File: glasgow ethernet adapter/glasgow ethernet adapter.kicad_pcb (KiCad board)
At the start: 4 copper layers, 61.7 x 49 mm, 59 parts, among them J1 Glasgow Port, J2 RJ45_Amphenol_RJMG201K21120FR, U1 MxL86110, Y1 25 MHz

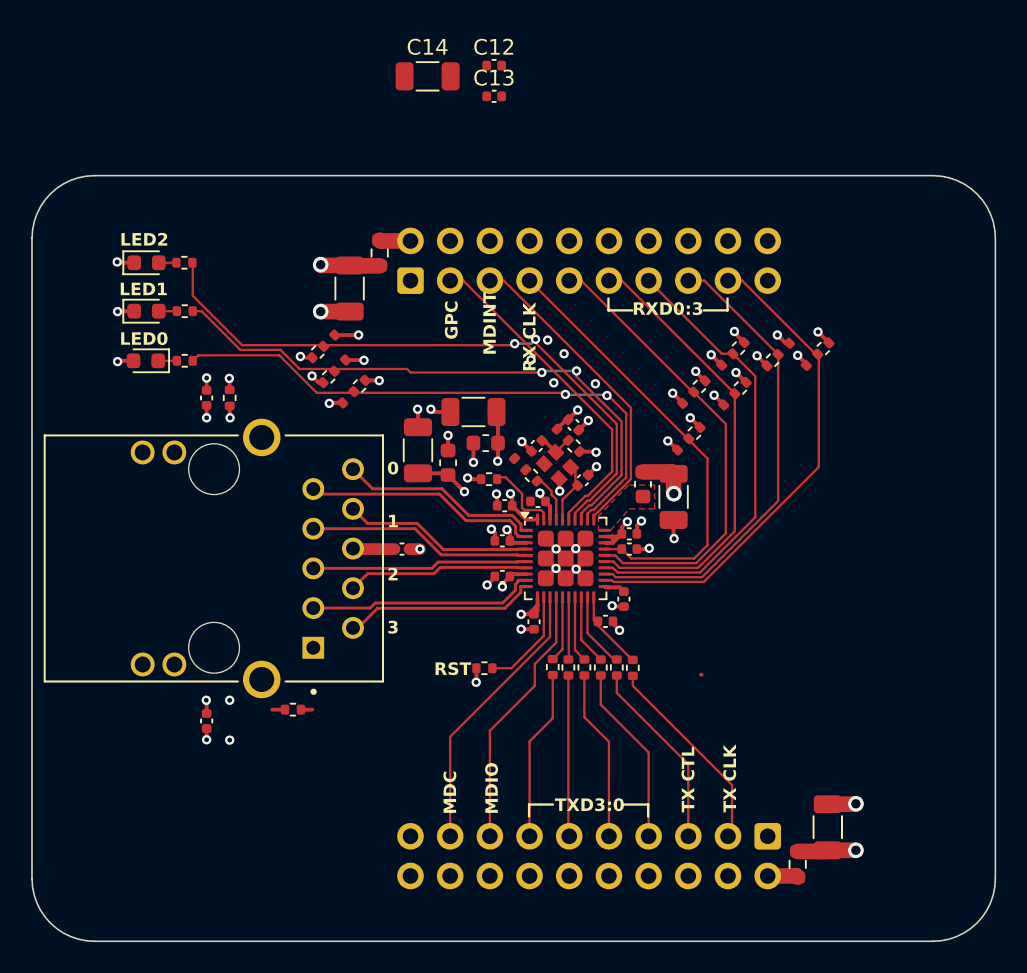
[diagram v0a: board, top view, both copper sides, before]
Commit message: remove configurable pulls on LEDs
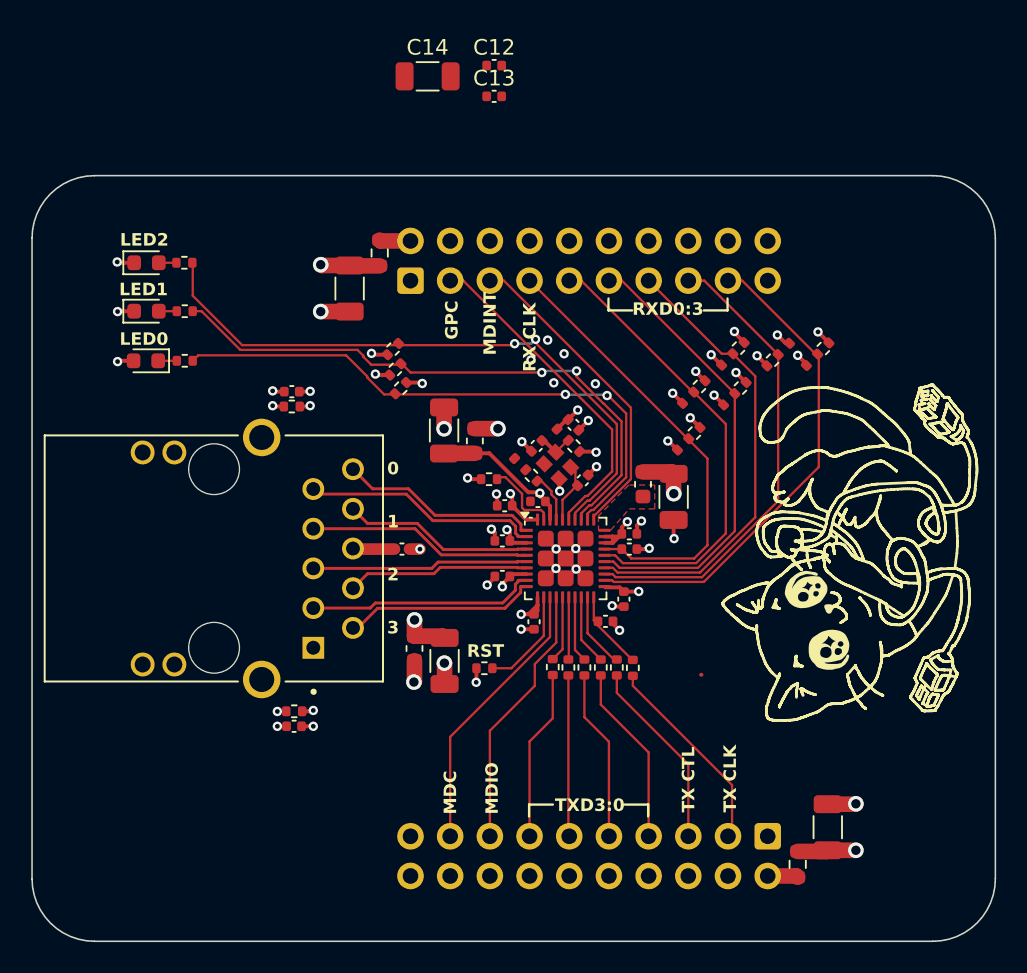
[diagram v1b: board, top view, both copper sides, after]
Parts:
- added REF**: cat, glasgow:cat, F.Cu at (181.5, 100.0)
- R3, R6, R9: footprint glasgow:R-3-Way_0402_1005Metric -> Resistor_SMD:R_0402_1005Metric
- moved C15 13.6 mm to (154.8, 106.6), turned to -90 degrees
- moved L2 12.1 mm to (152.8, 105.8), turned to 90 degrees
- moved C22 5.61 mm to (145.1, 110.7), turned to 0 degrees
- moved C27 5.46 mm to (145.0, 89.3), turned to 0 degrees
- moved R6 4.81 mm to (151.4, 86.6), turned to -135 degrees
- moved R3 4.29 mm to (151.6, 87.9), turned to -135 degrees
- moved R24 4.01 mm to (145.0, 90.3), turned to 0 degrees
- moved R9 2.65 mm to (151.9, 89.1), turned to 45 degrees
- moved C11 2.22 mm to (154.7, 91.8), turned to 90 degrees
- moved L3 0.71 mm to (156.7, 92.5), turned to -90 degrees
- moved R10 0.13 mm to (145.1, 109.8)
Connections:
- R3 pad 1: GND -> /CFG_LDO0
- R3 pad 2: /CFG_LDO0 -> GND
- R6 pad 1: GND -> /CFG_LDO1
- R6 pad 2: /CFG_LDO1 -> GND
- R9 pad 1: +3V3 -> /CFG_EXT
- R9 pad 2: /CFG_EXT -> +3V3
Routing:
- net +1V1: track 5.95 -> 27.1 mm, vias 2 -> 3
- net +3V3: track 25.5 -> 23.3 mm, vias 16 -> 14
- net C_GND: track 3.38 -> 2.59 mm
- net /AVDDL: track 19.5 -> 20.0 mm, vias 4 -> 3
- net GND: track 45.1 -> 44.9 mm, vias 44 -> 43
- removed copper zone on In2.Cu, net +1V1

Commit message: move things around
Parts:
- moved C13 53.2 mm to (178.6, 119.5), turned to -90 degrees
- moved C14 33.2 mm to (170.7, 97.7)
- moved C12 15.9 mm to (149.4, 81.9), turned to -90 degrees
- moved R11 5.74 mm to (153.6, 111.4)
- moved R9 5.05 mm to (147.9, 86.1), turned to 135 degrees
- moved C11 2.94 mm to (154.8, 94.8), turned to -90 degrees
- moved R6 2.88 mm to (150.1, 84.1), turned to 45 degrees
- moved R3 2.77 mm to (150.2, 85.5)
- moved C20 2.30 mm to (146.5, 81.9), turned to 180 degrees
- moved C10 1.41 mm to (170.6, 95.3), turned to 0 degrees
- moved C17 0.98 mm to (180.2, 117.2)
- moved L1 0.05 mm to (167.5, 95.2)
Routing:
- net +3V3: track 23.3 -> 36.0 mm, vias 14 -> 15
- net Net-(U1-RSTN): track 6.61 -> 12.2 mm
- net /PHYAD1: track 28.9 -> 33.7 mm
- net GND: track 44.9 -> 48.5 mm, vias 43 -> 47
- net +1V1: track 27.1 -> 30.4 mm
- net /RXD0: track 29.4 -> 32.6 mm
- net /RXD1: track 29.6 -> 32.8 mm
- net /PHYAD2: track 29.6 -> 32.4 mm
- net /PLLOFF: track 30.3 -> 32.9 mm
- net /AVDDL: track 20.0 -> 17.9 mm
- net /PHYAD0: track 31.7 -> 32.9 mm
- net Net-(R26-Pad2): track 0.15 -> 1.36 mm

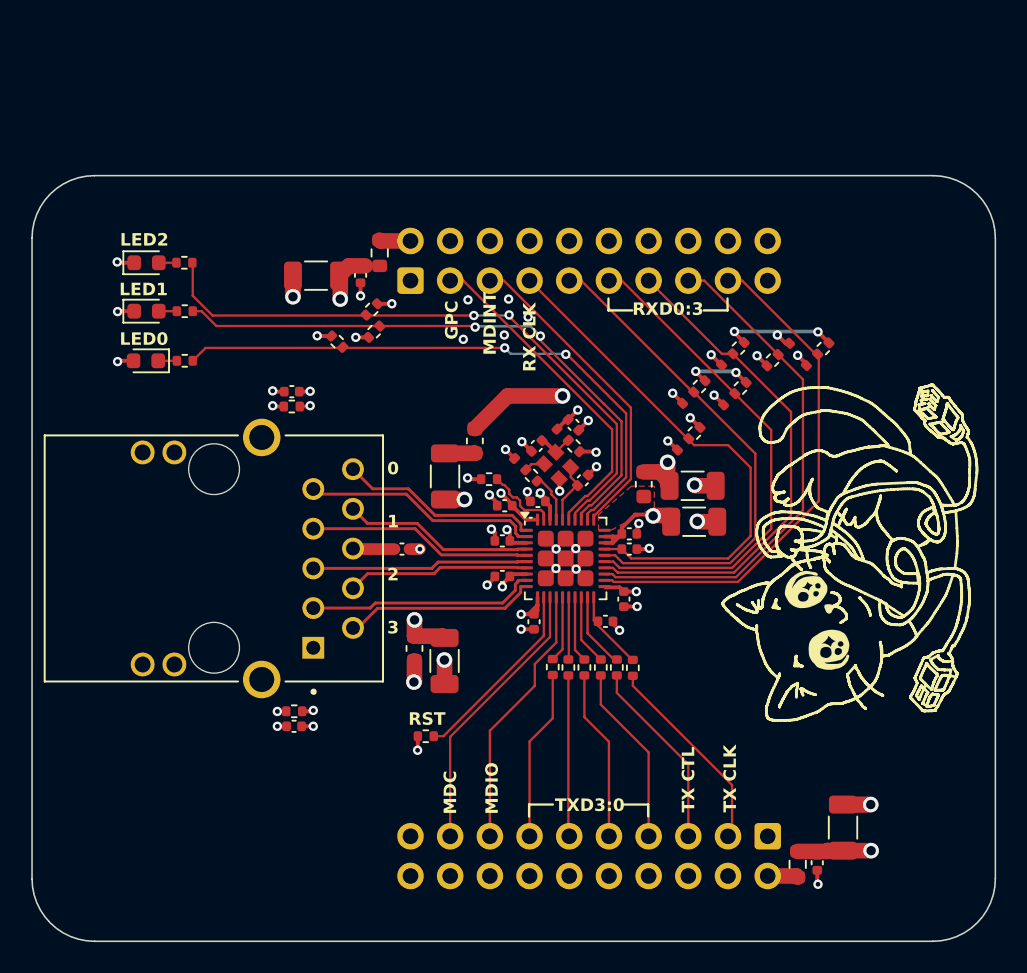
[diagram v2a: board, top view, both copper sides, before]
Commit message: increase fab tolerances, DRC fixes
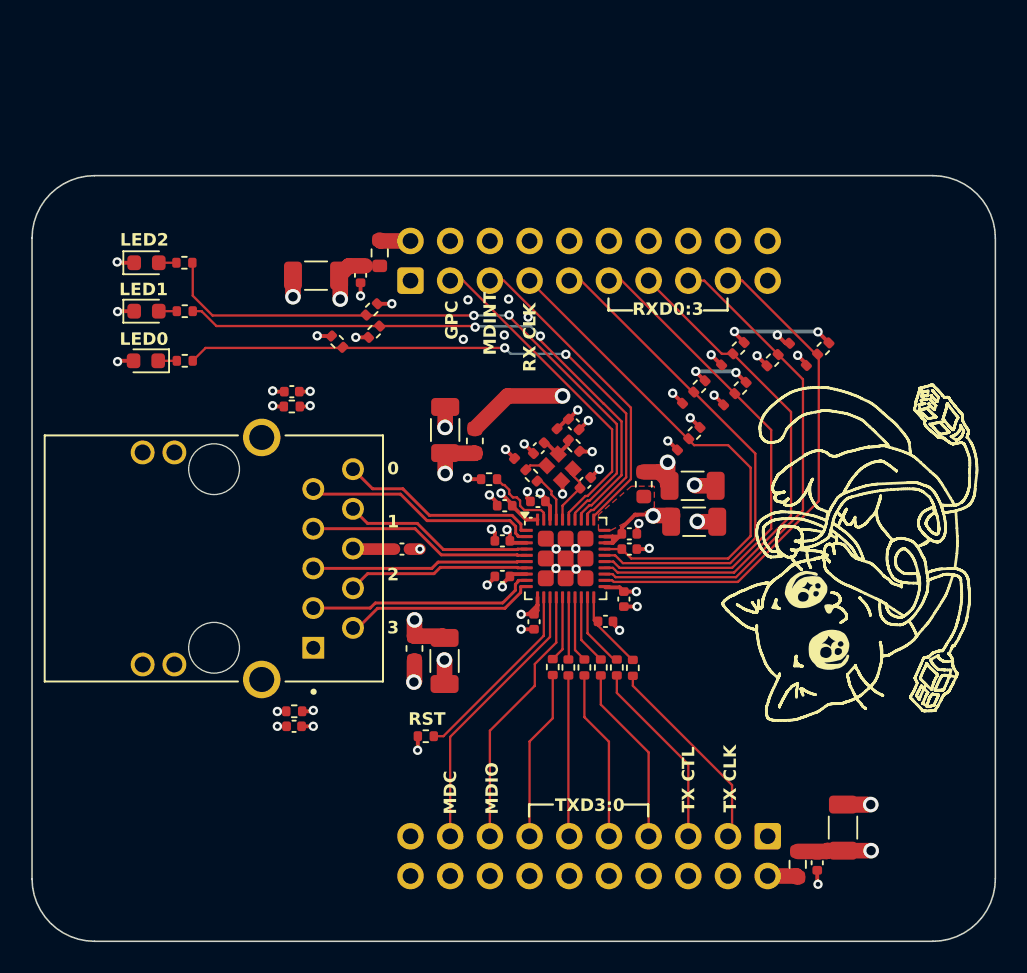
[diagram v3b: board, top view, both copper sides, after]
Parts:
- moved C11 2.97 mm to (154.8, 91.8), turned to 90 degrees
- moved C25 0.23 mm to (163.8, 95.2)
- moved Y1 0.20 mm to (162.1, 94.2)
- moved C26 0.19 mm to (160.8, 92.9)
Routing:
- net /AVDDL: track 17.9 -> 26.7 mm, vias 3 -> 4
- net C_GND: track 2.59 -> 3.16 mm

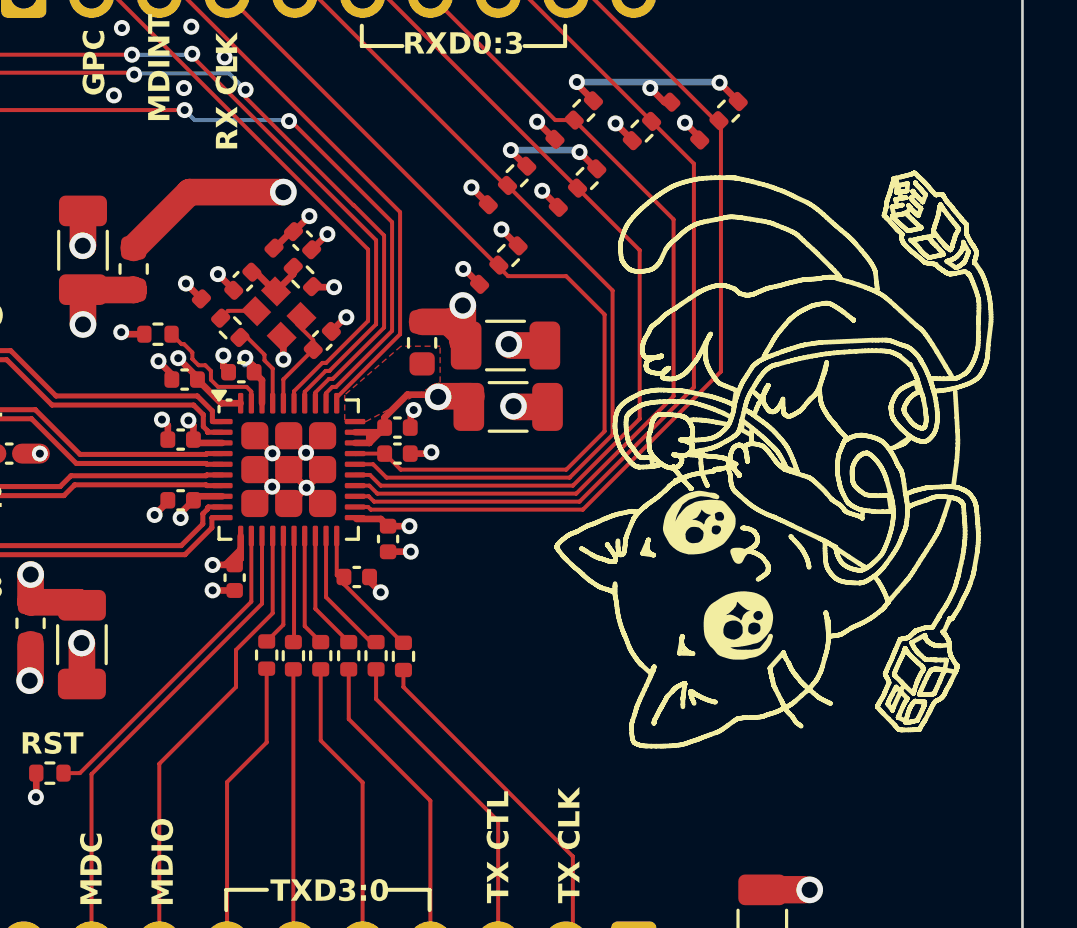
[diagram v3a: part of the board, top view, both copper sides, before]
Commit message: export fab outputs, add note on parts sourcing
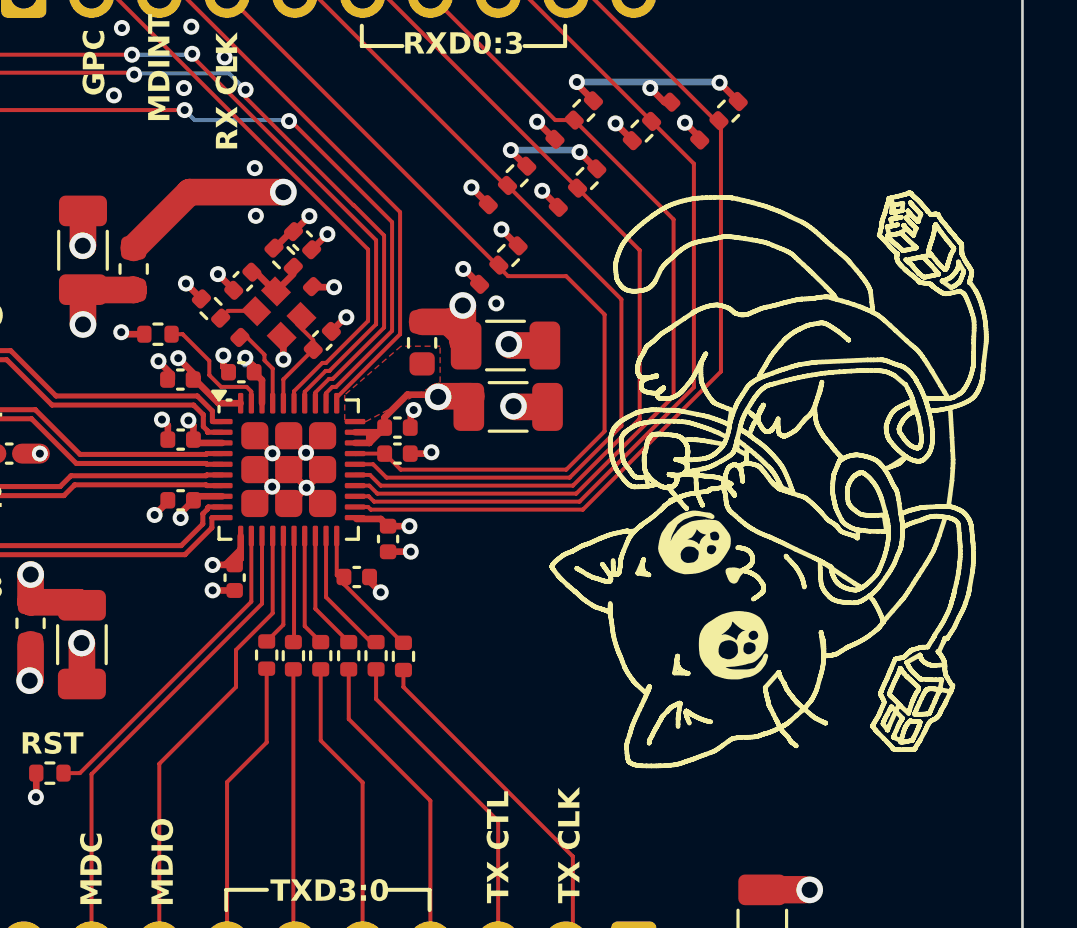
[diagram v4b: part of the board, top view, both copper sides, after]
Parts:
- moved R25 1.02 mm to (162.3, 92.1), turned to -45 degrees
- moved R26 1.02 mm to (159.6, 94.0), turned to -45 degrees
- moved REF** 0.76 mm to (181.3, 100.7)
- moved C5 0.16 mm to (158.4, 96.6)
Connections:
- R25 pad 1: GND -> +3V3
- R25 pad 3: +3V3 -> GND
- R26 pad 1: /XTAL_O -> +3V3
- R26 pad 3: +3V3 -> /XTAL_O
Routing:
- net +1V1: track 30.4 -> 31.4 mm
- net GND: vias 47 -> 50

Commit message: un-swap pins
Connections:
- J2 pad 10: /TRX1+ -> /TRX4-
- J2 pad 2: /TRX4- -> /TRX1+
- J2 pad 3: /TRX4+ -> /TRX1-
- J2 pad 4: /TRX3- -> /TRX2+
- J2 pad 5: /TRX3+ -> /TRX2-
- J2 pad 7: /TRX2- -> /TRX3+
- J2 pad 8: /TRX2+ -> /TRX3-
- J2 pad 9: /TRX1- -> /TRX4+
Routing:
- net /TRX4+: track 14.7 -> 20.4 mm, vias 0 -> 1
- net /TRX3-: track 11.7 -> 17.1 mm, vias 0 -> 1
- net /TRX4-: track 12.4 -> 17.8 mm, vias 0 -> 1
- net /TRX3+: track 13.8 -> 17.6 mm, vias 0 -> 1
- net /TRX1-: track 15.2 -> 18.8 mm
- net /TRX2-: track 14.8 -> 16.9 mm, vias 0 -> 1
- net /TRX1+: track 13.0 -> 14.7 mm
- net /TRX2+: track 12.2 -> 12.7 mm, vias 0 -> 1
